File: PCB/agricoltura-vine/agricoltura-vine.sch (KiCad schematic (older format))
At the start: 0 parts

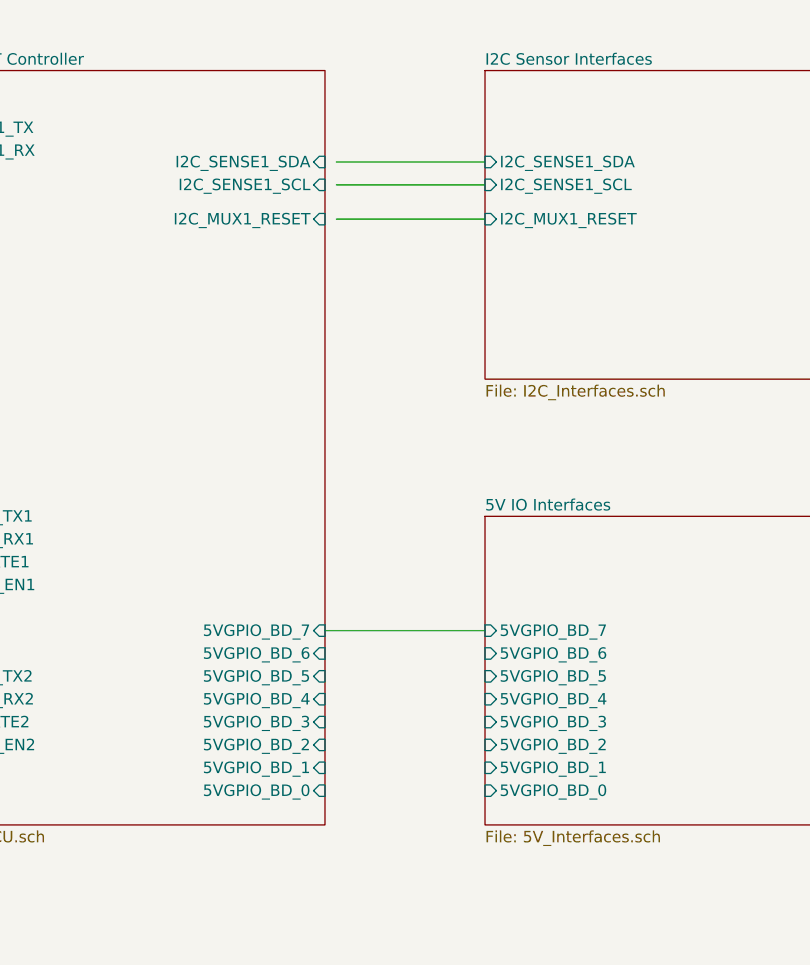
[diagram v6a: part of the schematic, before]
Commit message: Big Update
Dropped 8 5V outputs in favor of two relays. Ditched microchip IO expander for a Ti one that does level conversion for outputs, eliminates Ti bidriectional converter and 74 line driver from design, simplifying everything.
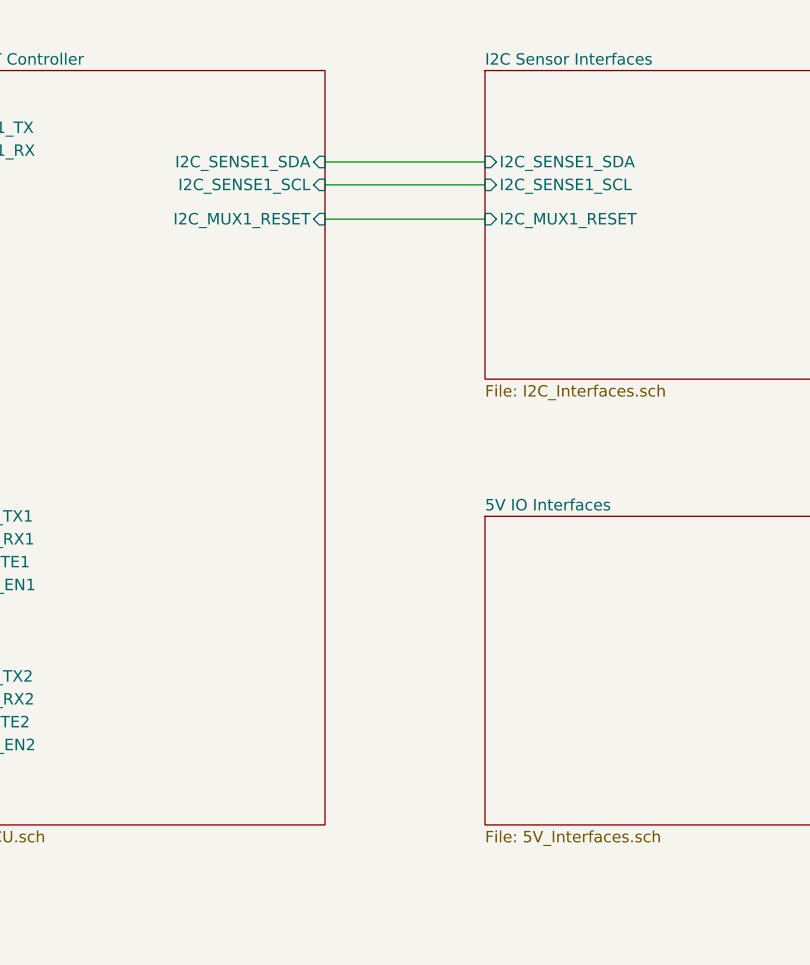
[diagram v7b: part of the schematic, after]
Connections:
- wire segments 21 -> 20
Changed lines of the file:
@@
 F20 "RS485_RE2" I L 4700 5050 50
 F21 "RS485_TERM_EN2" I L 4700 4950 50
-F22 "5VGPIO_BD_0" I R 6650 5150 50
-F23 "5VGPIO_BD_1" I R 6650 5050 50
-F24 "5VGPIO_BD_2" I R 6650 4950 50
-F25 "5VGPIO_BD_3" I R 6650 4850 50
-F26 "5VGPIO_BD_4" I R 6650 4750 50
-F27 "5VGPIO_BD_5" I R 6650 4650 50
-F28 "5VGPIO_BD_6" I R 6650 4550 50
-F29 "5VGPIO_BD_7" I R 6650 4450 50
 $EndSheet
 $Sheet
@@
 	3800 4750 4700 4750
 Wire Wire Line
-	7350 2650 6700 2650
+	7350 2650 6650 2650
 Wire Wire Line
-	6700 2500 7350 2500
+	6650 2500 7350 2500
 Wire Wire Line
-	6700 2400 7350 2400
+	6650 2400 7350 2400
 Wire Wire Line
 	3500 2350 4700 2350
@@
 Text Notes 4250 1350 0    200  ~ 40
 Agricoltura Vine 0.1a
-$Sheet
-S 7350 3950 1900 1350
-U 5EF943A9
-F0 "5V IO Interfaces" 50
-F1 "5V_Interfaces.sch" 50
-F2 "5VGPIO_BD_0" I L 7350 5150 50
-F3 "5VGPIO_BD_1" I L 7350 5050 50
-F4 "5VGPIO_BD_2" I L 7350 4950 50
-F5 "5VGPIO_BD_3" I L 7350 4850 50
-F6 "5VGPIO_BD_4" I L 7350 4750 50
-F7 "5VGPIO_BD_5" I L 7350 4650 50
-F8 "5VGPIO_BD_6" I L 7350 4550 50
-F9 "5VGPIO_BD_7" I L 7350 4450 50
-$EndSheet
 Wire Wire Line
 	4700 4850 3800 4850
@@
 Wire Wire Line
 	3800 4250 4700 4250
-Wire Wire Line
-	6650 4450 7350 4450
+$Sheet
+S 7350 3950 1900 1350
+U 5EF943A9
+F0 "5V IO Interfaces" 50
+F1 "5V_Interfaces.sch" 50
+$EndSheet
 $EndSCHEMATC

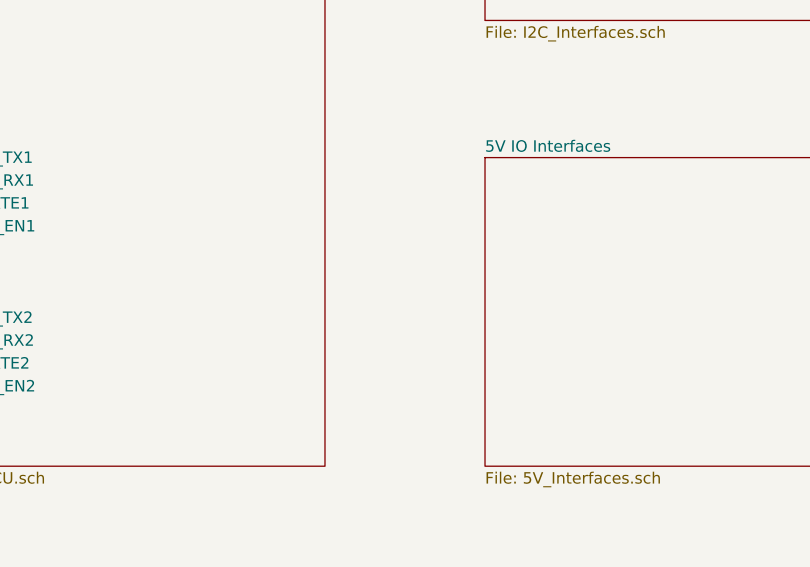
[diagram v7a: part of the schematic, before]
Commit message: Relay Driver Circuit, Board Size Change
Added the Relay driver circuitry, increased size of board tobetter acccomodate relays, figuredout the powerplane topology to get 5Vs where it needs to go.
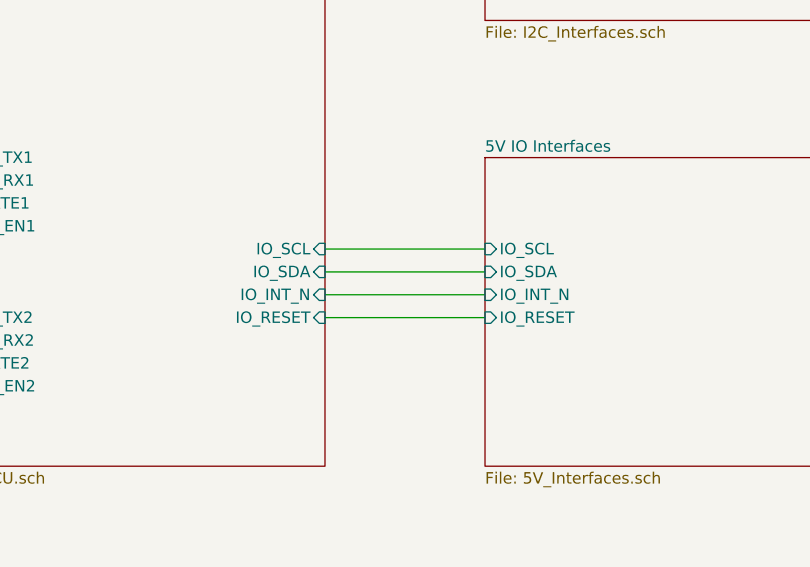
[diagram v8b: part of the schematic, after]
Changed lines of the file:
@@
 F20 "RS485_RE2" I L 4700 5050 50
 F21 "RS485_TERM_EN2" I L 4700 4950 50
+F22 "IO_SCL" I R 6650 4350 50
+F23 "IO_SDA" I R 6650 4450 50
+F24 "IO_INT_N" I R 6650 4550 50
+F25 "IO_RESET" I R 6650 4650 50
 $EndSheet
 $Sheet
@@
 F0 "5V IO Interfaces" 50
 F1 "5V_Interfaces.sch" 50
+F2 "IO_SCL" I L 7350 4350 50
+F3 "IO_SDA" I L 7350 4450 50
+F4 "IO_INT_N" I L 7350 4550 50
+F5 "IO_RESET" I L 7350 4650 50
 $EndSheet
+Wire Wire Line
+	7350 4350 6650 4350
+Wire Wire Line
+	7350 4450 6650 4450
+Wire Wire Line
+	7350 4550 6650 4550
+Wire Wire Line
+	6650 4650 7350 4650
 $EndSCHEMATC
